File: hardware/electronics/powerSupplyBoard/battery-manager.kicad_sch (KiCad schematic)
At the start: 44 parts, among them J5 S3B-XH-SM4-TB, Q2 DMT3006LPS, Q3 NXV90EP, Q4 DMT3006LPS, Q5 2N7002NXAK, U4 AP7361E, U5 BQ40Z50-R2, U6 TCA9509

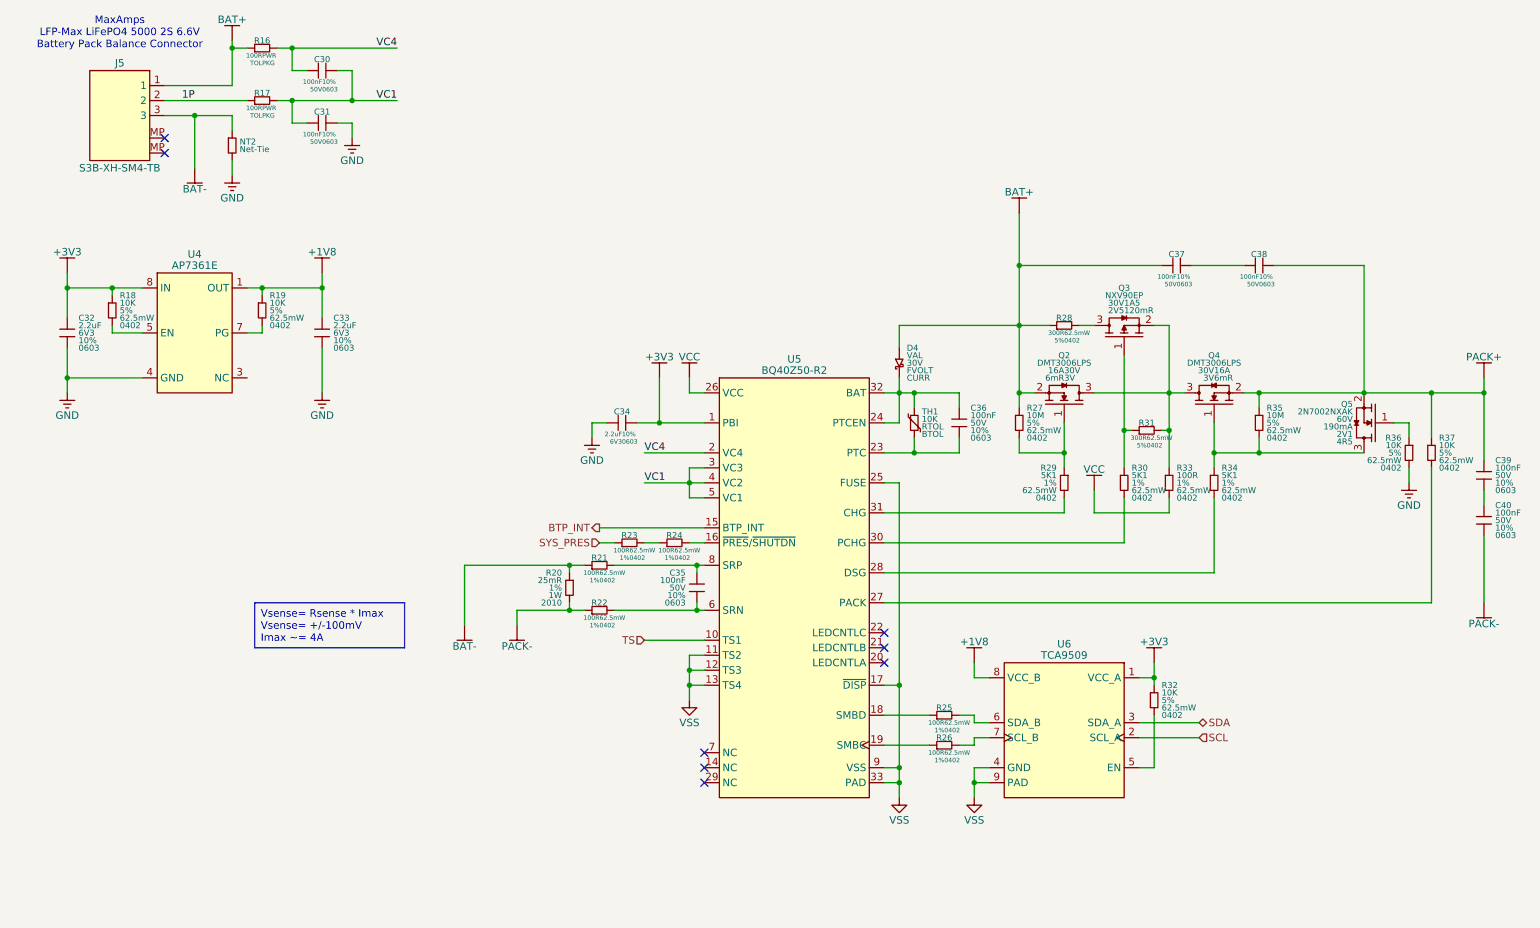
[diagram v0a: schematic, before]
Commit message: finished schematic and net labels
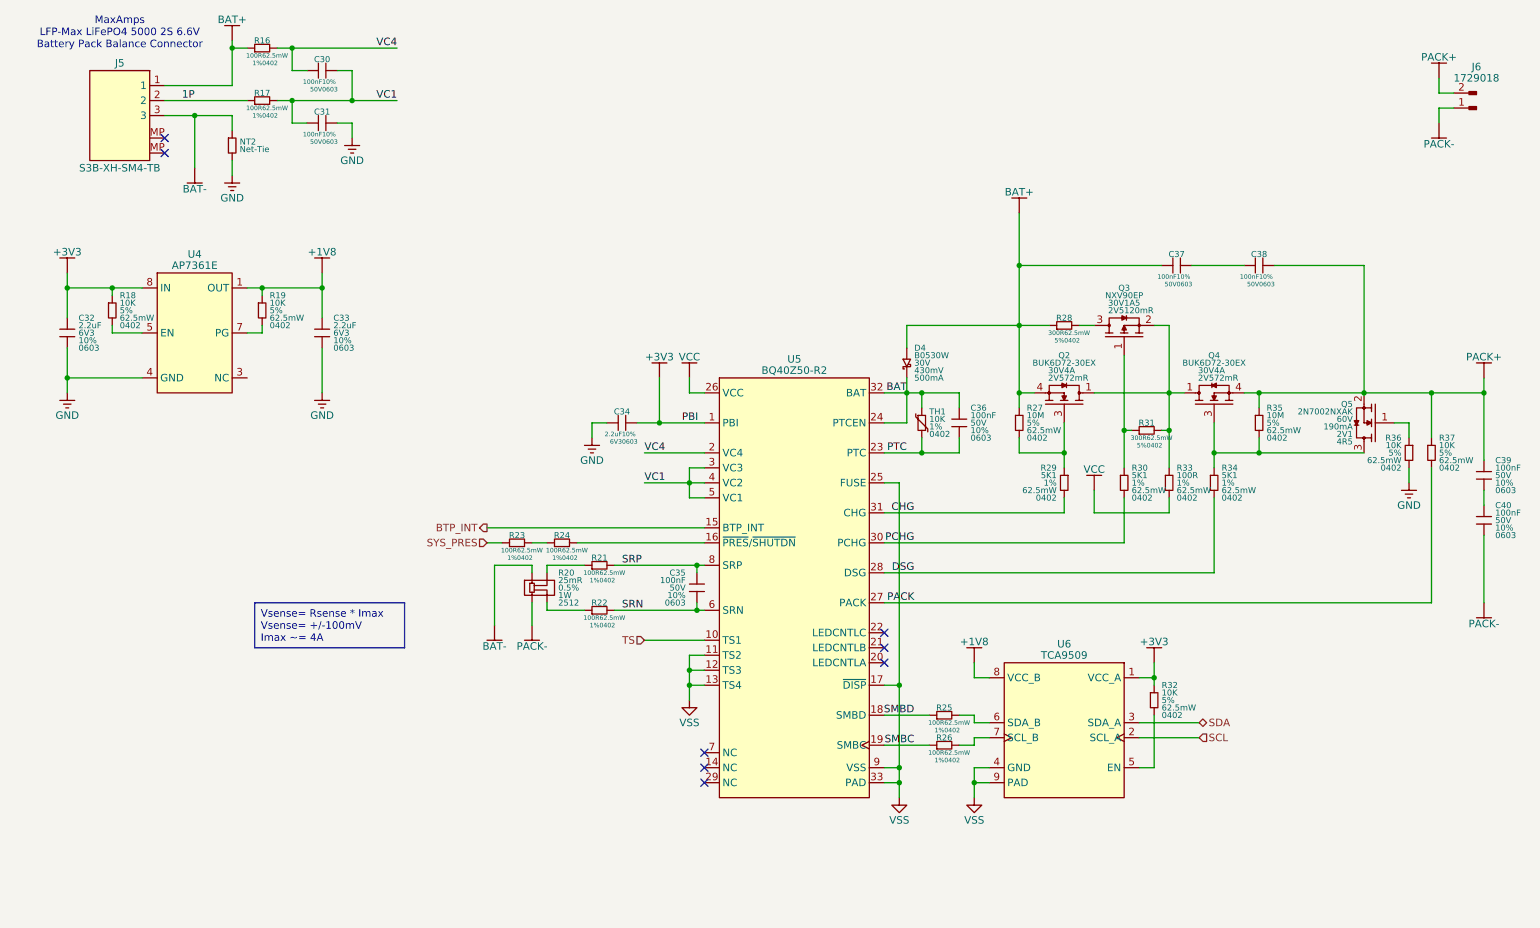
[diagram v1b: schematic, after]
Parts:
- removed Q2, Q4: DMT3006LPS, symbol lib_sch:NMOS_GSD
- removed R20: 25mR, lib_fp:WSLHP2010, symbol lib_sch:R
- added J6: 1729018, lib_fp:5mmTerminalBlock, symbol lib_sch:Conn_01x02_Pin
- added Q2, Q4: BUK6D72-30EX, lib_fp:UDFN6P65_200X200X65L30X25N, symbol lib_sch:NMOS_DGS
- added R20: 25mR, lib_fp:WSK2512, symbol DS-Passives:R_sense
- D4: value VAL -> B0530W; footprint (none) -> lib_fp:SOD123; Current CURR -> 500mA; DKPN (none) -> B0530W-FDICT-ND; Forward Voltage FVOLT -> 430mV; MPN (none) -> B0530W-7-F; Manufacturer (none) -> Diodes Incorporated
- R16, R17: footprint (none) -> lib_fp:CRCW0402; DKPN (none) -> 541-100LCT-ND; MPN (none) -> CRCW0402100RFKED; Package PKG -> 0402; Power Rating PWR -> 62.5mW; Tolerance TOL -> 1%
- TH1: footprint (none) -> lib_fp:SON2P65_100X60X50L50X25N; B Value Tolerance BTOL -> (none); DKPN (none) -> 296-53530-1-ND; MPN (none) -> TMP6131QDECRQ1; Manufacturer (none) -> Texas Instruments; Package (none) -> 0402; Resistance Tolerance RTOL -> 1%
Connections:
- net BAT+: now also Q2.4, Q2.8
- net BAT-: now also R20.3; no longer R21.1
- net PACK+: now also J6.2, Q4.4, Q4.8
- net PACK-: now also J6.1, R20.1; no longer R22.1
- net BAT: now reaches C36.1, D4.2, TH1.1, U5.24 (PTCEN), U5.32 (BAT)
- net PTC: now reaches C36.2, TH1.2, U5.23 (PTC)
- net at R27.2, R29.1: now also Q2.3
- net at Q3.2, R31.2, R33.1: now also Q2.1, Q2.2, Q2.5, Q2.6, Q2.7, Q4.1, Q4.2, Q4.5, Q4.6, Q4.7
- net PACK: now reaches R37.2, U5.27 (PACK)
- net PCHG: now reaches R30.2, U5.30 (PCHG)
- net at Q5.3, R34.1, R35.2: now also Q4.3
- net DSG: now reaches R34.2, U5.28 (DSG)
- net SRN: now reaches C35.2, R22.2, U5.6 (SRN)
- net SMBD: now reaches R25.1, U5.18 (SMBD)
- net SRP: now reaches C35.1, R21.2, U5.8 (SRP)
- net CHG: now reaches R29.2, U5.31 (CHG)
- net SMBC: now reaches R26.1, U5.19 (SMBC)
- new net: R20.2, R22.1
- new net: R20.4, R21.1
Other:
- moved on the sheet: D4, R23, R24, TH1

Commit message: added battery connector and updated date
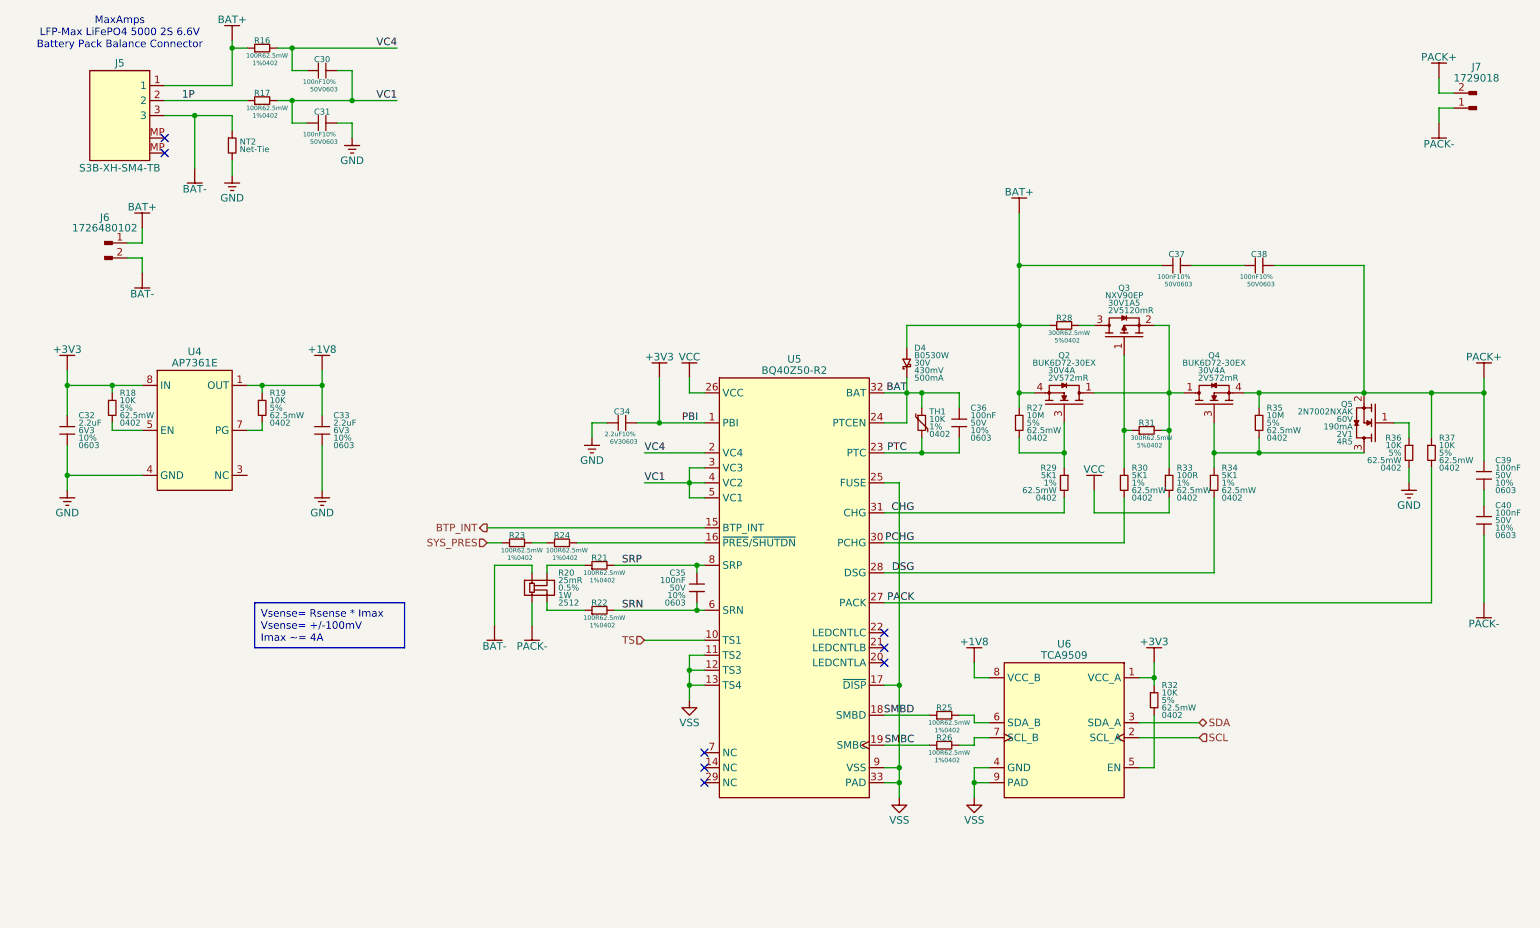
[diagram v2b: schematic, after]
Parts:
- added J6: 1726480102, lib_fp:1726480102, symbol lib_sch:Conn_01x02_Pin
- renumbered J6 to J7
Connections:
- net BAT+: now also J6.1
- net BAT-: now also J6.2
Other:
- moved on the sheet: C32, C33, R18, R19, U4

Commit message: added output vreg and made changed from design review
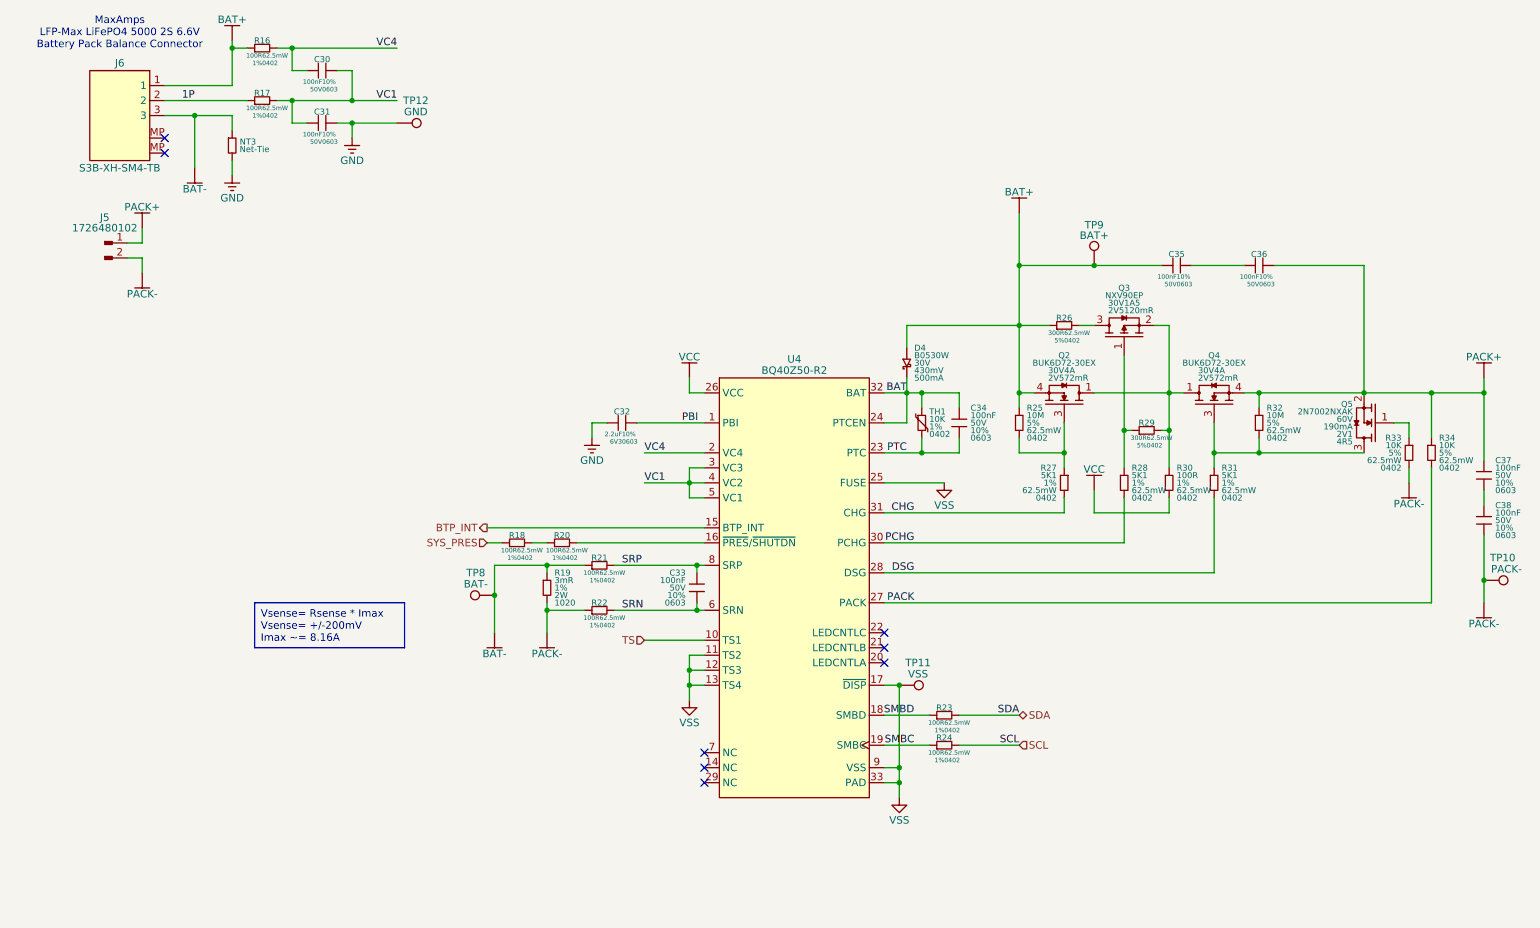
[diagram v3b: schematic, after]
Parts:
- removed C32, C33: 2.2uF, lib_fp:MLCC0603, symbol lib_sch:C
- removed J7: 1729018, lib_fp:5mmTerminalBlock, symbol lib_sch:Conn_01x02_Pin
- removed R18, R32: 10K, lib_fp:CRCW0402, symbol lib_sch:R
- removed R20: 25mR, lib_fp:WSK2512, symbol DS-Passives:R_sense
- removed U4: AP7361E, lib_fp:UDFN8P65_300X300X60L25X45L, symbol lib_sch:AP7361E
- removed U6: TCA9509, lib_fp:RVH0008A, symbol lib_sch:TCA9509
- added TP10: PACK-, lib_fp:TP_1mm, symbol lib_sch:TestPoint
- added TP11: VSS, lib_fp:TP_1mm, symbol lib_sch:TestPoint
- added TP12: GND, lib_fp:TP_1mm, symbol lib_sch:TestPoint
- added TP8: BAT-, lib_fp:TP_1mm, symbol lib_sch:TestPoint
- added TP9: BAT+, lib_fp:TP_1mm, symbol lib_sch:TestPoint
- R19: value 10K -> 3mR; footprint lib_fp:CRCW0402 -> lib_fp:WSL1020; DKPN 541-10KJCT-ND -> 541-10044-1-ND; MPN CRCW040210K0JNED -> WSL10203L000FEA; Package 0402 -> 1020; Power Rating 62.5mW -> 2W; Tolerance 5% -> 1%
- renumbered C34 to C32, C35 to C33, C36 to C34, C37 to C35, C38 to C36, C39 to C37, C40 to C38, J6 to J5, J5 to J6, NT2 to NT3, R23 to R18, R24 to R20, R25 to R23, R26 to R24, R27 to R25, R28 to R26, R29 to R27, R30 to R28, R31 to R29, R33 to R30, R34 to R31, R35 to R32, R36 to R33, R37 to R34, U5 to U4
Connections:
- net +1V8 is gone; now on net BAT-: R19.1
- net BAT+: now also TP9.1; no longer J5.1
- net BAT-: now also R21.1, TP8.1; no longer J5.2
- net GND: now also TP12.1; no longer R33.2
- net PACK+: now also J5.1
- net PACK-: now also J5.2, R19.2, R22.1, R33.2, TP10.1
- net SCL: now also R24.2
- net SDA: now also R23.2
- net VSS: now also TP11.1
- net +3V3 renamed PBI
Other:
- title: (none) -> Battery Manager

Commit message: fixed ERC
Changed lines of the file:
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@@
 	(title_block
 		(title "Battery Manager")
-		(date "2024-12-17")
+		(date "2024-12-22")
 		(rev "02")
 		(comment 2 "PROTOTYPE")
@@
 	)
 	(junction
+		(at 29.21 52.07)
+		(diameter 0)
+		(color 0 0 0 0)
+	)
+	(junction
 		(at 256.54 106.68)
 		(diameter 0)
@@
 	)
 	(junction
+		(at 116.84 80.01)
+		(diameter 0)
+		(color 0 0 0 0)
+	)
+	(junction
 		(at 161.29 74.93)
 		(diameter 0)
@@
 	)
 	(junction
+		(at 190.5 95.25)
+		(diameter 0)
+		(color 0 0 0 0)
+	)
+	(junction
 		(at 123.19 104.14)
 		(diameter 0)
@@
 	(wire
 		(pts
-			(xy 113.03 80.01) (xy 124.46 80.01)
+			(xy 113.03 80.01) (xy 116.84 80.01)
 		)
 		(stroke
@@
 	(wire
 		(pts
+			(xy 31.75 52.07) (xy 29.21 52.07)
+		)
+		(stroke
+			(width 0)
+			(type default)
+		)
+	)
+	(wire
+		(pts
 			(xy 114.3 85.09) (xy 124.46 85.09)
 		)
@@
 	(wire
 		(pts
+			(xy 116.84 80.01) (xy 124.46 80.01)
+		)
+		(stroke
+			(width 0)
+			(type default)
+		)
+	)
+	(wire
+		(pts
 			(xy 158.75 63.5) (xy 177.8 63.5)
 		)
@@
 	)
 	(symbol
+		(lib_id "DS-Power:PWR_FLAG")
+		(at 31.75 52.07 270)
+		(unit 1)
+		(exclude_from_sim no)
+		(in_bom yes)
+		(on_board yes)
+		(dnp no)
+		(property "Reference" "#FLG05"
+			(at 31.75 52.07 0)
+			(effects
+				(font
+					(size 1.27 1.27)
+				)
+				(hide yes)
+			)
+		)
+		(property "Value" "PWR_FLAG"
+			(at 34.29 52.07 90)
+			(do_not_autoplace yes)
+			(effects
+				(font
+					(size 1.27 1.27)
+				)
+				(justify left)
+			)
+		)
+		(property "Footprint" ""
+			(at 31.75 52.07 0)
+			(effects
+				(font
+					(size 1.27 1.27)
+				)
+				(hide yes)
+			)
+		)
+		(property "Datasheet" ""
+			(at 31.75 52.07 0)
+			(effects
+				(font
+					(size 1.27 1.27)
+				)
+				(hide yes)
+			)
+		)
+		(property "Description" "Special symbol for telling ERC where power comes from"
+			(at 31.75 52.07 0)
+			(effects
+				(font
+					(size 1.27 1.27)
+				)
+				(hide yes)
+			)
+		)
+		(pin "1"
+		)
+		(instances
+			(project "powerSupplyBoard"
+				(path "/6f3ae1d2-e925-4178-b812-ea14ec542b6c/04580fb9-8d30-4e40-859b-31ba28a834a9"
+					(reference "#FLG05")
+					(unit 1)
+				)
+			)
+		)
+	)
+	(symbol
 		(lib_id "lib_sch:R")
 		(at 243.84 85.09 0)
@@
 	)
 	(symbol
+		(lib_id "DS-Power:PWR_FLAG")
+		(at 116.84 80.01 0)
+		(unit 1)
+		(exclude_from_sim no)
+		(in_bom yes)
+		(on_board yes)
+		(dnp no)
+		(fields_autoplaced yes)
+		(property "Reference" "#FLG04"
+			(at 116.84 80.01 0)
+			(effects
+				(font
+					(size 1.27 1.27)
+				)
+				(hide yes)
+			)
+		)
+		(property "Value" "PWR_FLAG"
+			(at 116.84 76.2 0)
+			(do_not_autoplace yes)
+			(effects
+				(font
+					(size 1.27 1.27)
+				)
+			)
+		)
+		(property "Footprint" ""
+			(at 116.84 80.01 0)
+			(effects
+				(font
+					(size 1.27 1.27)
+				)
+				(hide yes)
+			)
+		)
+		(property "Datasheet" ""
+			(at 116.84 80.01 0)
+			(effects
+				(font
+					(size 1.27 1.27)
+				)
+				(hide yes)
+			)
+		)
+		(property "Description" "Special symbol for telling ERC where power comes from"
+			(at 116.84 80.01 0)
+			(effects
+				(font
+					(size 1.27 1.27)
+				)
+				(hide yes)
+			)
+		)
+		(pin "1"
+		)
+		(instances
+			(project ""
+				(path "/6f3ae1d2-e925-4178-b812-ea14ec542b6c/04580fb9-8d30-4e40-859b-31ba28a834a9"
+					(reference "#FLG04")
+					(unit 1)
+				)
+			)
+		)
+	)
+	(symbol
 		(lib_id "lib_sch:NMOS_DGS")
 		(at 185.42 74.93 0)
@@
 		(property "Reference" "J5"
 			(at 22.86 45.212 0)
-			(do_not_autoplace yes)
 			(effects
 				(font
@@
 		(property "Value" "1726480102"
 			(at 22.86 46.99 0)
-			(do_not_autoplace yes)
 			(effects
 				(font
@@
 		(pin "2"
 		)
-		(pin "MP"
+		(pin "MP1"
 		)
-		(pin "MP"
+		(pin "MP2"
 		)
 		(pin "1"
@@
 					(unit 1)
 				)
+			)
+		)
+	)
+	(symbol
+		(lib_id "DS-Power:PWR_FLAG")
+		(at 190.5 95.25 180)
+		(unit 1)
+		(exclude_from_sim no)
+		(in_bom yes)
+		(on_board yes)
+		(dnp no)
+		(fields_autoplaced yes)
+		(property "Reference" "#FLG07"
+			(at 190.5 95.25 0)
+			(effects
+				(font
+					(size 1.27 1.27)
+				)
+				(hide yes)
+			)
+		)
+		(property "Value" "PWR_FLAG"
+			(at 190.5 99.06 0)
+			(do_not_autoplace yes)
+			(effects
+				(font
+					(size 1.27 1.27)
+				)
+			)
+		)
+		(property "Footprint" ""
+			(at 190.5 95.25 0)
+			(effects
+				(font
+					(size 1.27 1.27)
+				)
+				(hide yes)
+			)
+		)
+		(property "Datasheet" ""
+			(at 190.5 95.25 0)
+			(effects
+				(font
+					(size 1.27 1.27)
+				)
+				(hide yes)
+			)
+		)
+		(property "Description" "Special symbol for telling ERC where power comes from"
+			(at 190.5 95.25 0)
+			(effects
+				(font
+					(size 1.27 1.27)
+				)
+				(hide yes)
+			)
+		)
+		(pin "1"
+		)
+		(instances
+			(project "powerSupplyBoard"
+				(path "/6f3ae1d2-e925-4178-b812-ea14ec542b6c/04580fb9-8d30-4e40-859b-31ba28a834a9"
+					(reference "#FLG07")
+					(unit 1)
+				)

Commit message: changes from design review
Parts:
- added BT1, BT2, BT3: ~, symbol DS-Batteries:Battery
- added NT4: Net-Tie, lib_fp:NetTie-2_SMD_Pad2.0mm, symbol lib_sch:NT
- NT3: footprint lib_fp:CRCW2010 -> lib_fp:NetTie-2_SMD_Pad2.0mm; DKPN 541-0.0WCT-ND -> (none); MPN CRCW20100000Z0EF -> (none); Manufacturer Vishay Dale -> (none)
- TP10: value PACK- -> CHG-
- TP8: value BAT- -> PACK-
- TP9: value BAT+ -> PACK+
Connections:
- net 1P: now also BT2.2, BT3.1
- net BAT+: no longer C35.1, D4.1, Q2.4, Q2.8, R25.1, R26.1, TP9.1
- net BAT-: no longer R19.1, R21.1, TP8.1
- net GND: now also R19.2, R22.1, NT4.1
- net PACK+: now also C35.1, D4.1, Q2.4, Q2.8, R25.1, R26.1, TP9.1, BT1.1, BT2.1; no longer C36.2, C37.1, Q4.4, Q4.8, Q5.2, R32.1, R34.1
- net PACK-: now also R19.1, R21.1, TP8.1, BT1.2, BT3.2; no longer C38.2, R19.2, R22.1, R33.2, TP10.1
- new net CHG+: C36.2, C37.1, Q4.4, Q4.8, Q5.2, R32.1, R34.1
- new net CHG-: C38.2, NT4.2, R33.2, TP10.1
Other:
- note added: "Balance Connector"
- note added: "Battery Connector"
- note added: "Virtual "Pack""
